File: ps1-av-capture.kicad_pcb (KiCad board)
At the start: 4 copper layers, 100 x 80 mm, 237 parts, among them J1 AV_PIGTAIL, J2 USB3_B, J3 USB_C_AUDIO, J4 JTAG, J5 UART, SW1 RESET, U1 TVP7002PZP, U10 TLV75733PDBVR, U11 TLV75533PDBVR, U12 PCM2903CDBR, U2 CYUSB3014-BZXI, U3 24LC1025-I/SN, U4 24LC1025-I/SN, U5 TPS563201DDCR, U6 TPS563201DDCR, U7 TPS563201DDCR, U8 TLV75519PDBVR, U9 TLV75519PDBVR, X1 27MHz, Y1 19.2MHz, Y2 12MHz

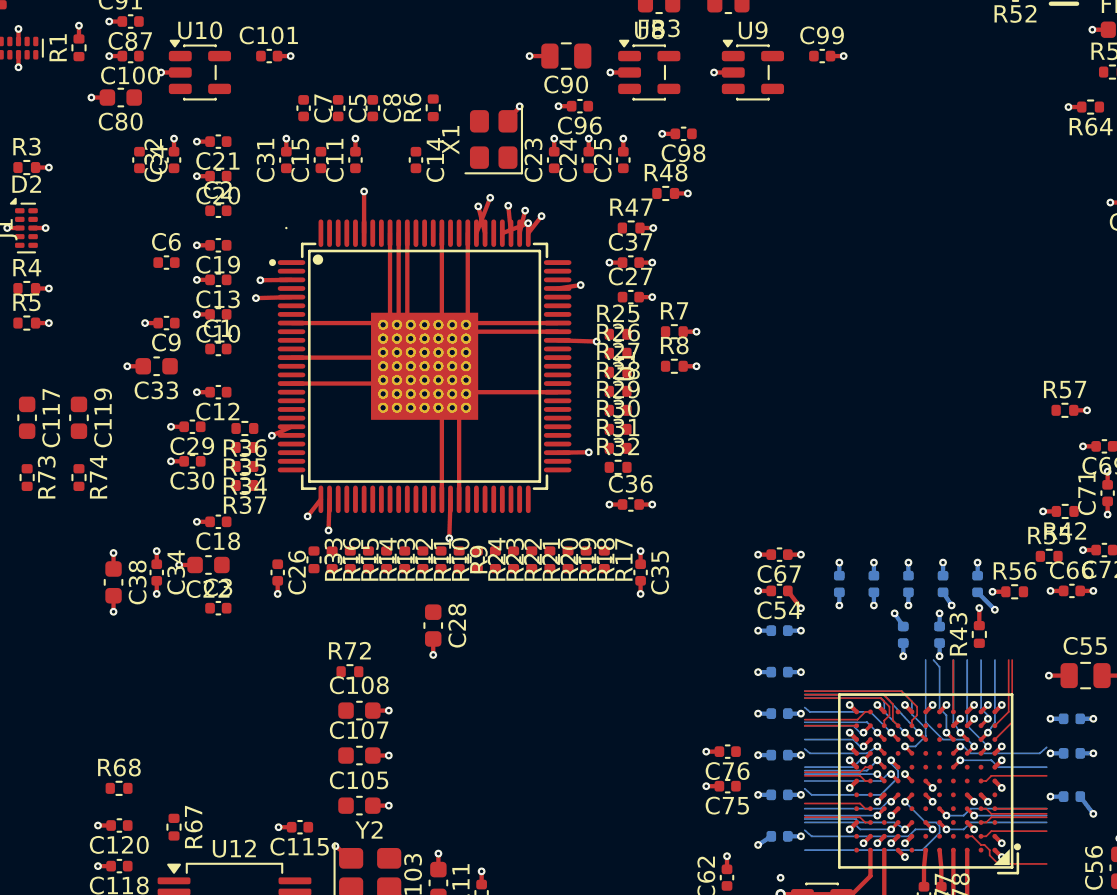
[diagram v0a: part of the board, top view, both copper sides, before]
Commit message: Layout: GPIF bundle routed, 29 of 29 VD nets TVP7002 -> FX3
The seven nets that never routed were not losing on congestion: every one
stopped after a few thousand A* expansions with the search space exhausted.
Four leave the escape box on B.Cu at x=55, 0.2 mm apart, and face the B.Cu
+1V2 decap column 1.5 mm west with its plane vias; the router allowed no
layer change inside the neckdown skirt, so they were sealed in. Vias are now
allowed there (GPIF_VIA_IN_NECK), every via keeps 0.4 mm hole-to-hole from
every other, and each escape end gets a short reserved exit.
Also: the sync 22Rs moved into the row under U1 (left of DATACLK).

DRC: no copper errors, no unconnected VD_ net. Lengths 15.5-52.5 mm.
check_geometry still flags the router's grid staircases (SHORT/ACUTE) on
these nets; cleanup is the next step.
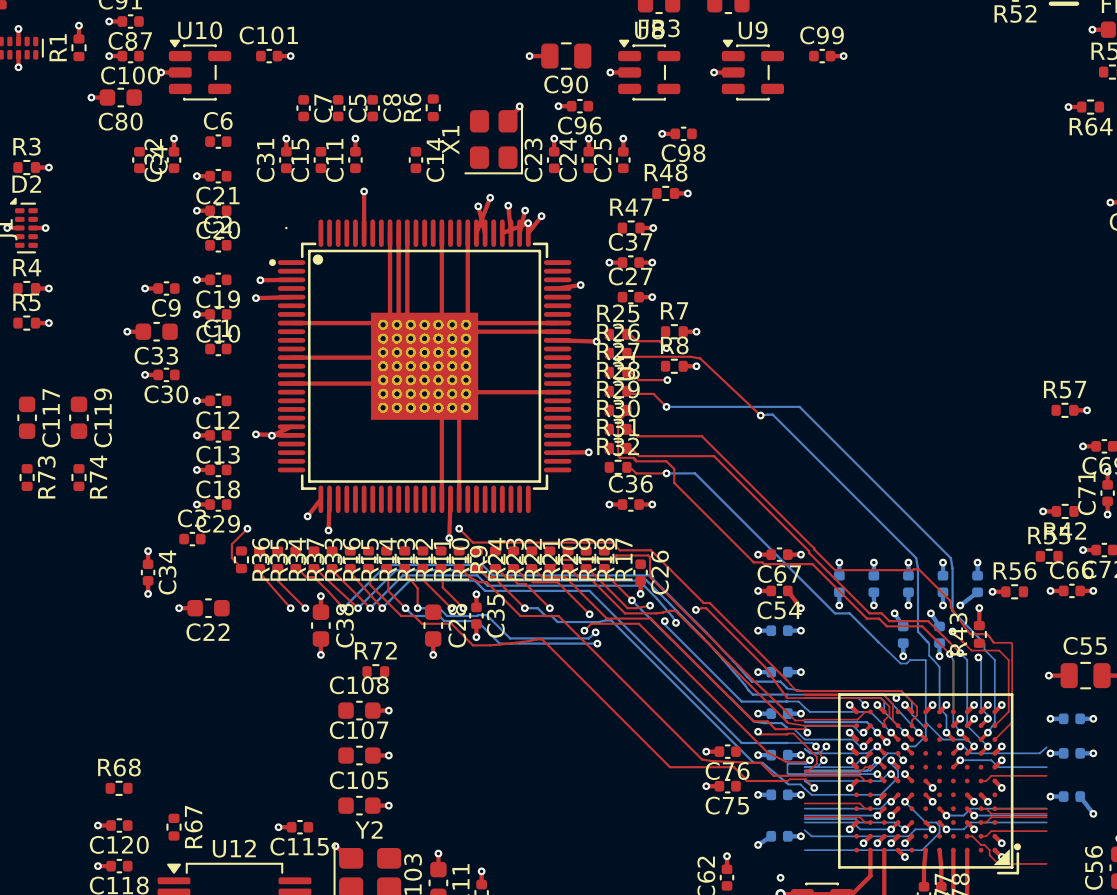
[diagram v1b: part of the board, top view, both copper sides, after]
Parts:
- moved C26 21.0 mm to (145.5, 137.9)
- moved C38 12.3 mm to (127.0, 141.0)
- moved C35 9.82 mm to (136.0, 140.4)
- moved C13 9.00 mm to (121.1, 130.0)
- moved C6 7.62 mm to (121.1, 113.0)
- moved R36 7.60 mm to (122.4, 137.2), turned to -90 degrees
- moved R35 6.56 mm to (123.5, 137.2), turned to -90 degrees
- moved R34 5.72 mm to (124.5, 137.2), turned to -90 degrees
- moved C30 5.22 mm to (118.1, 126.5)
- moved R37 5.21 mm to (125.5, 137.2), turned to -90 degrees
- moved C29 4.74 mm to (121.1, 134.0)
- moved C3 4.27 mm to (119.6, 136.0)
- moved C18 3.00 mm to (121.1, 132.0)
- moved C22 2.50 mm to (120.5, 140.0)
- moved C19 2.00 mm to (121.1, 121.0)
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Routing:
- net VD_FID: track 7.55 -> 60.1 mm, vias 1 -> 3
- net VD_HS: track 6.70 -> 52.2 mm, vias 0 -> 2
- net VD_B6: track 5.01 -> 46.5 mm, vias 1 -> 4
- net VD_VS: track 8.10 -> 46.3 mm, vias 0 -> 2
- net VD_B9: track 4.98 -> 40.8 mm, vias 1 -> 4
- net VD_B8: track 4.13 -> 38.7 mm, vias 1 -> 4
- net VD_SOG: track 10.8 -> 44.9 mm, vias 1 -> 2
- net VD_PCLK: track 8.12 -> 41.1 mm, vias 1 -> 2
- net VD_B7: track 5.73 -> 37.9 mm, vias 1 -> 2
- net VD_B5: track 3.92 -> 34.8 mm, vias 0 -> 3
- net VD_R2: track 4.13 -> 34.5 mm, vias 1 -> 3
- net VD_B3: track 4.77 -> 34.2 mm, vias 1 -> 4
- net VD_R5: track 4.89 -> 34.2 mm, vias 1 -> 2
- net VD_R4: track 4.13 -> 33.2 mm, vias 0 -> 2
- net VD_R7: track 5.01 -> 33.5 mm
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
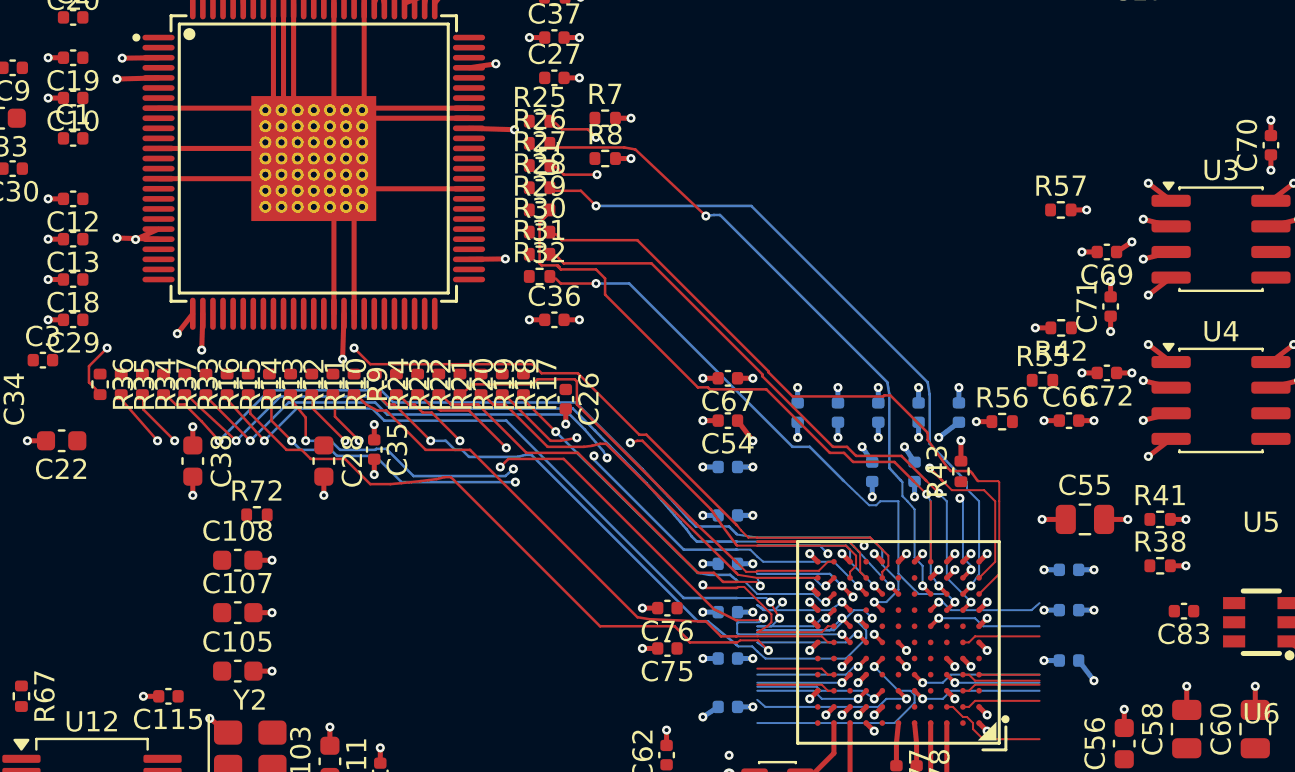
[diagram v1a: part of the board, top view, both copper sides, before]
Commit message: gpif_route: collapse grid staircases and reversals
One simplify() for both routers: vertex/staircase deletion, 45-degree corner
chamfers, neck-edge vertex kept on the edge, exact DRC-clearance checks.
Sealed escape ends branch off their stub (stub trimmed) instead of doubling back.
VD_* check_geometry: SHORT 53->7, ACUTE 17->0, OVERLAP 7->0, DANGLING 18->0;
29/29 routed, DRC 0 violations; 840.8->813.2 mm, 43->46 vias.
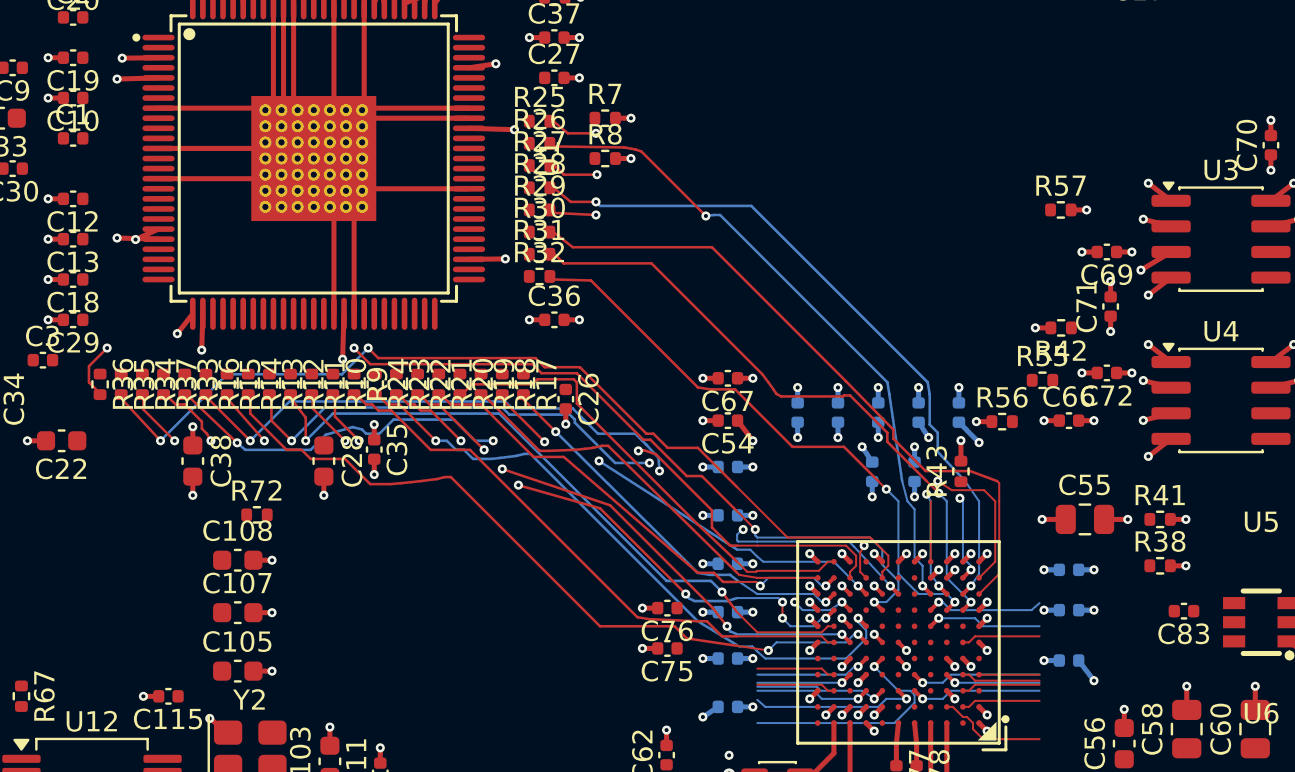
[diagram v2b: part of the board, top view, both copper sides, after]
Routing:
- net VD_FID: track 60.1 -> 48.0 mm, vias 3 -> 2
- net VD_G3: track 31.6 -> 21.3 mm, vias 3 -> 2
- net VD_B6: track 46.5 -> 36.3 mm, vias 4 -> 3
- net VD_HS: track 52.2 -> 42.6 mm
- net VD_B8: track 38.7 -> 35.2 mm, vias 4 -> 6
- net VD_B3: track 34.2 -> 30.7 mm
- net VD_R6: track 32.3 -> 29.5 mm, vias 2 -> 3
- net VD_SOG: track 44.9 -> 47.1 mm, vias 2 -> 4
- net VD_B9: track 40.8 -> 39.1 mm
- net VD_B7: track 37.9 -> 36.6 mm
- net VD_PCLK: track 41.1 -> 42.3 mm, vias 2 -> 4
- net VD_R2: track 34.5 -> 33.5 mm
- net VD_B5: track 34.8 -> 33.8 mm, vias 3 -> 2
- net VD_G8: track 27.1 -> 26.4 mm
- net VD_G6: track 24.1 -> 23.4 mm
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
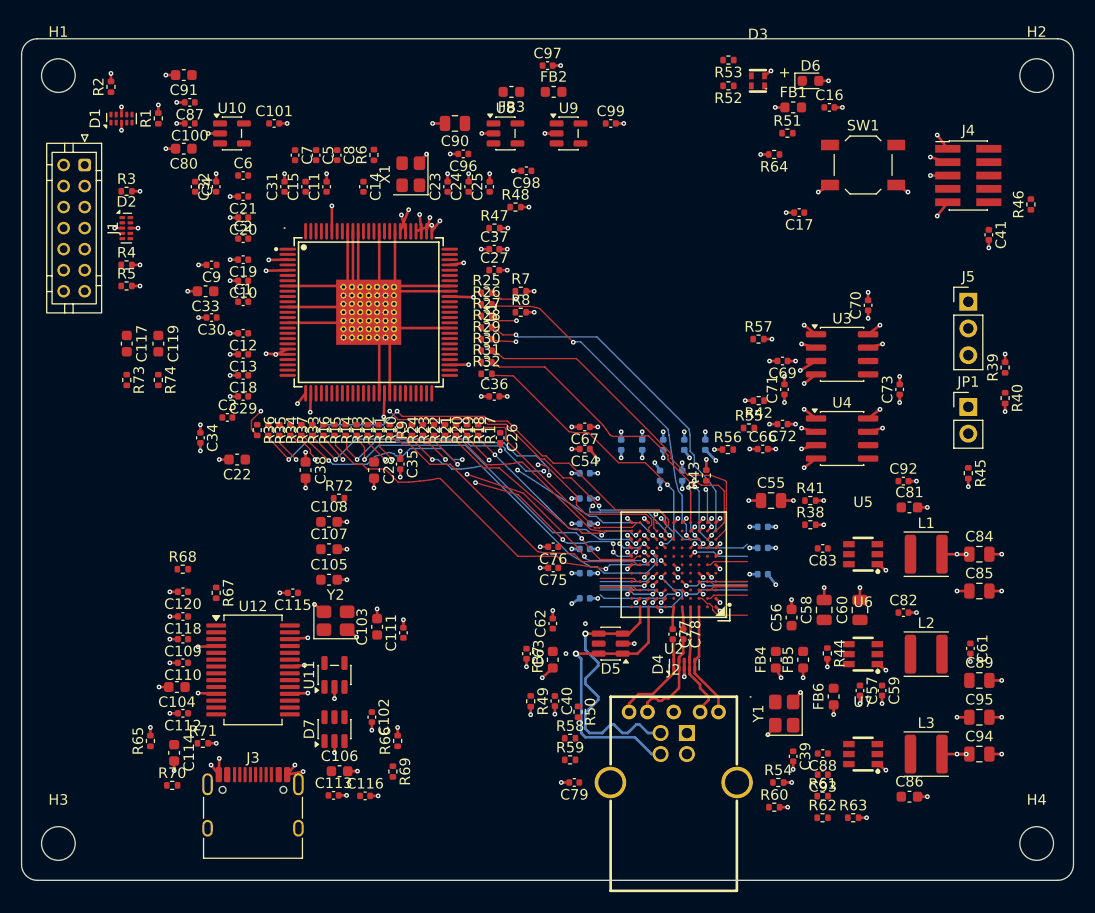
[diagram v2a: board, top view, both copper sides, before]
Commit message: fanout: one stub per plane pad
A pad that already holds a same-net via (L3/C94, L1/C84) or sits under a fanned pad
(J3 A1/B12) is left on that via; a stub may not run over a same-net via or stub.
Clears the 2 ACUTE GND and 2 OVERLAP +1V2/+3V3 findings. Unconnected 283 -> 283.
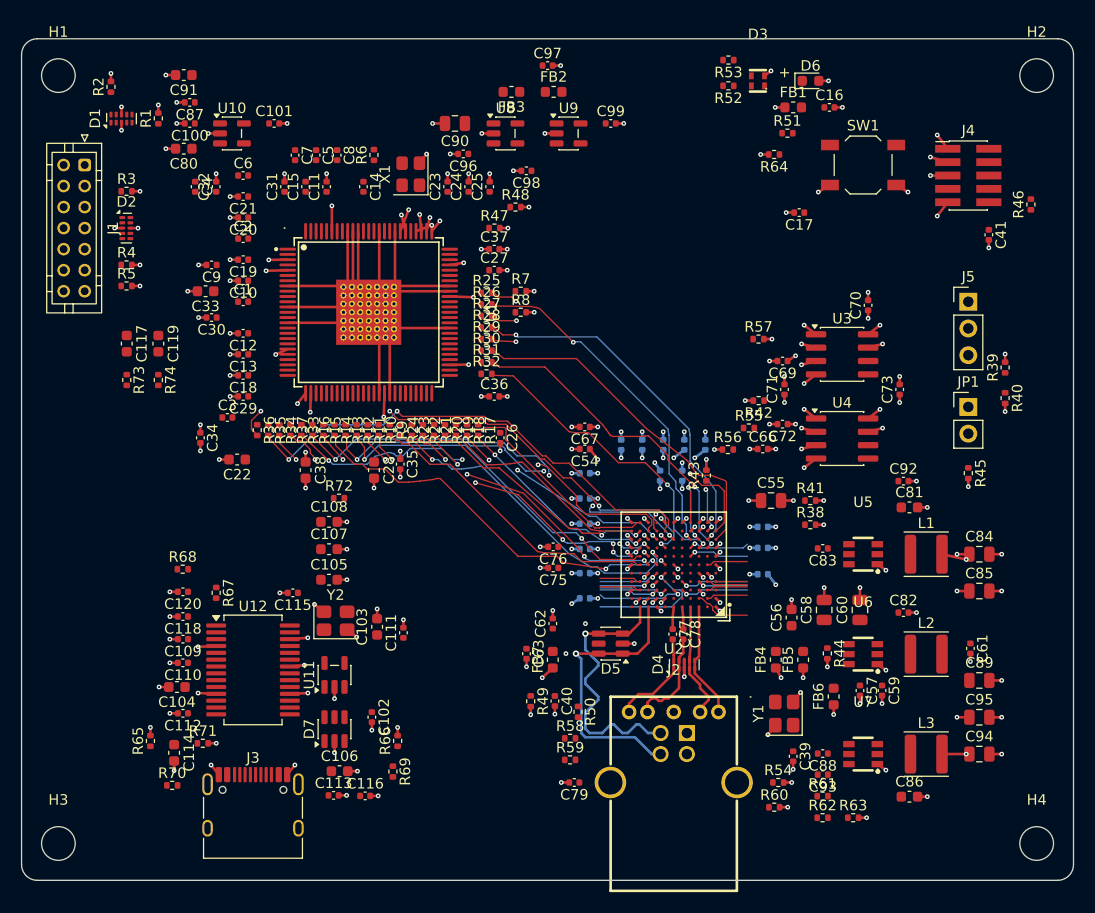
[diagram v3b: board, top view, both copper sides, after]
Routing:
- net GND: track 245.9 -> 241.0 mm, vias 194 -> 191
- net +1V2: track 23.5 -> 22.3 mm, vias 27 -> 26
- net VD_R2: track 33.5 -> 32.9 mm

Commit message: p2p_route: supplies, plane stitches, point-to-point signals
New last build stage: A* on F.Cu/B.Cu per net, FX3 supply balls dogboned first.
Unconnected 283 -> 112: supplies 105 -> 3, plane nets 13 -> 5, FX3_U3TX/RX 6 -> 0,
crystals/I2C/FSLC/22R/reset/LED/PMODE 72 -> 17. DRC 0 violations.
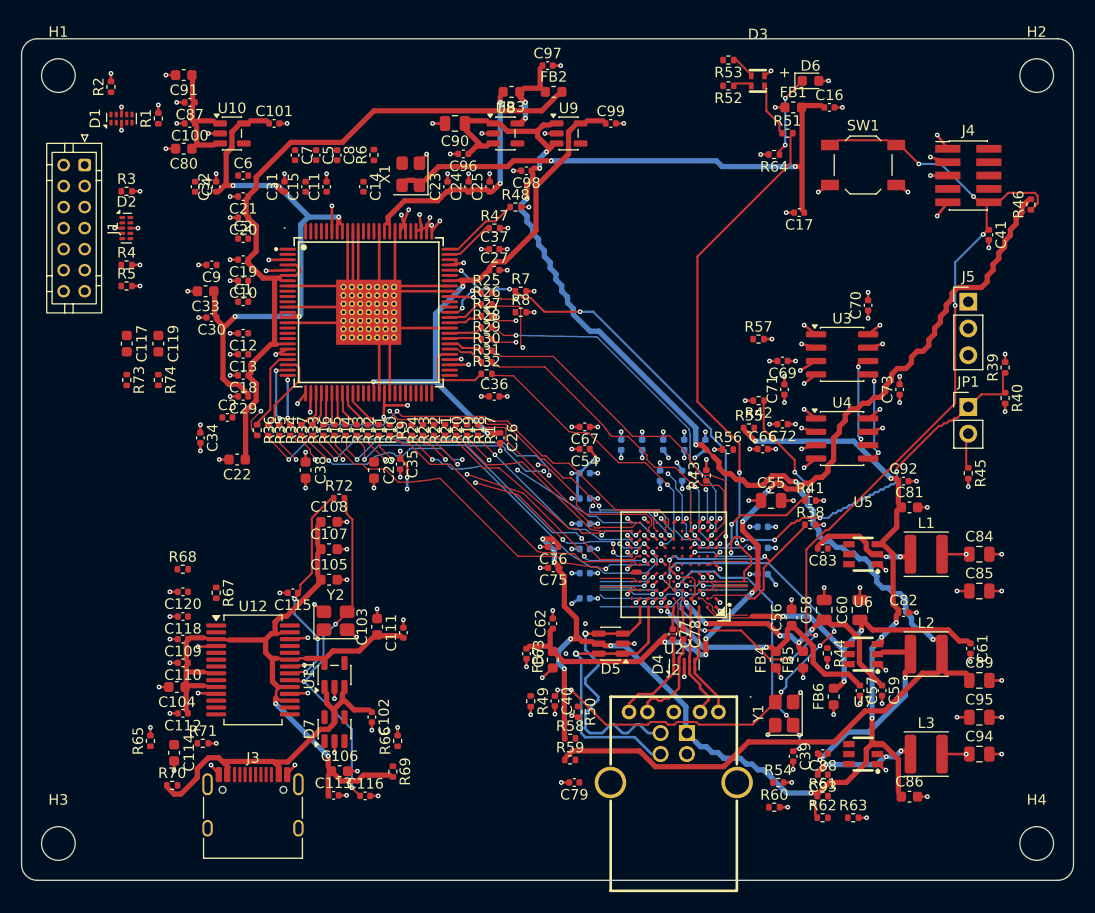
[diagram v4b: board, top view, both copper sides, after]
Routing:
- net +2V5: track 0.00 -> 126.0 mm, vias 0 -> 6
- net VBUS: track 0.00 -> 113.3 mm, vias 0 -> 11
- net FX3_CVDDQ: track 0.00 -> 87.3 mm, vias 0 -> 6
- net FX3_RESETn: track 6.53 -> 90.8 mm, vias 1 -> 8
- net TVP_AVDD: track 0.00 -> 62.8 mm
- net +3V3_AUD: track 0.00 -> 57.8 mm, vias 0 -> 2
- net FX3_XO: track 6.57 -> 58.5 mm, vias 1 -> 7
- net +3V3A: track 0.00 -> 50.0 mm, vias 0 -> 5
- net LED_R: track 3.00 -> 51.6 mm, vias 0 -> 2
- net OSC_VDD: track 0.00 -> 48.1 mm, vias 0 -> 2
- net +1V9D: track 0.00 -> 46.6 mm, vias 0 -> 3
- net TVP_RESETn: track 3.92 -> 46.7 mm, vias 0 -> 4
- net FX3_PMODE0: track 5.73 -> 38.8 mm, vias 1 -> 6
- net FX3_U3RX: track 0.00 -> 31.7 mm, vias 0 -> 3
- net AUD_XO: track 0.00 -> 30.8 mm, vias 0 -> 3
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
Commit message: gpif_route: VD_HS escapes north, bundle kept off In2 planes
VD_HS leaves K8 north on F.Cu (38.1 mm, 0 vias; was west, 41.2 mm, 2 vias). In2 is
closed to the bundle over +1V2/+3V3 outside the escape box; F.Cu U1->22R paths kept clear.
vs a fresh 49b060d build: GPIF 29/29 both, DRC 0 copper, unconnected 111 -> 96,
In2 breaks >=0.25 mm2 +1V2 5 -> 1, +3V3 4 -> 1, VD_ SHORT 5 -> 2. TVP_HSOUT now unrouted.
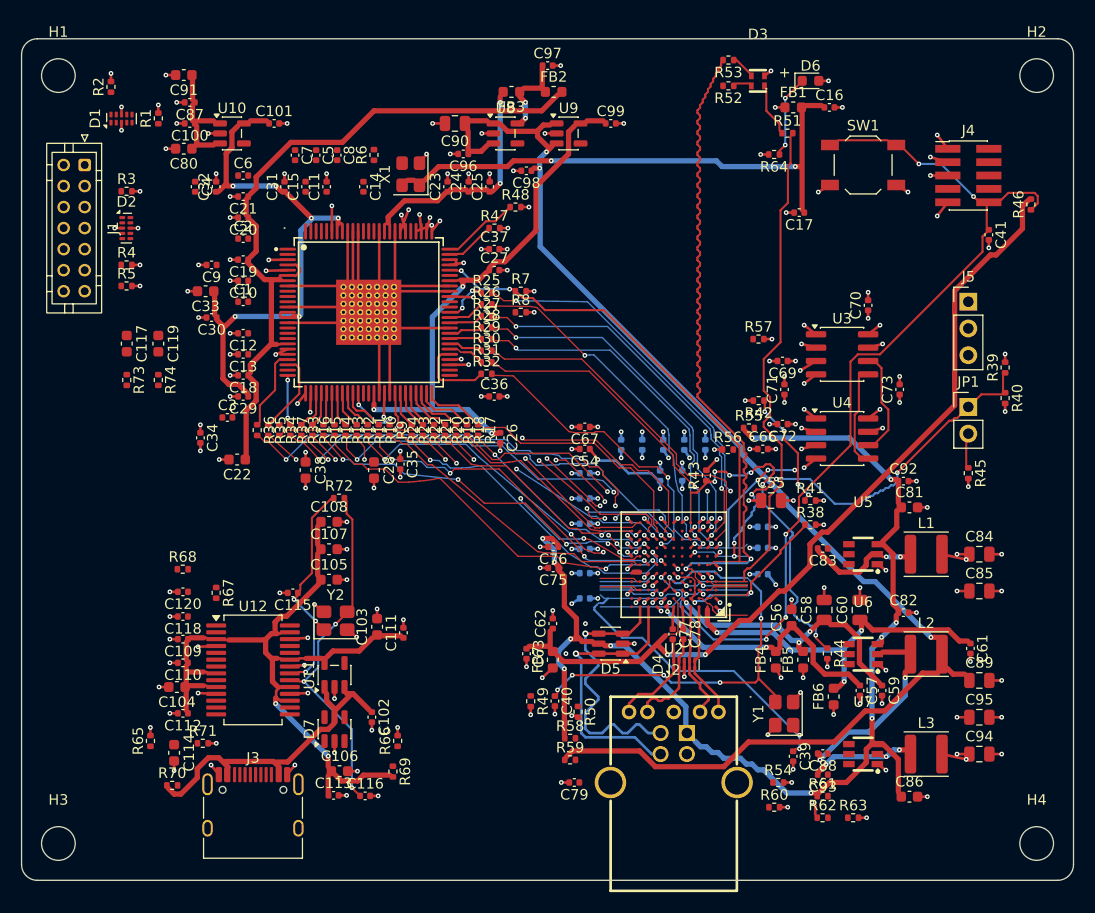
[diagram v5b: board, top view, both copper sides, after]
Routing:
- net LED_B: track 4.77 -> 70.1 mm, vias 1 -> 3
- net FX3_PMODE2: track 3.00 -> 33.4 mm, vias 0 -> 6
- net FX3_XO: track 58.5 -> 49.1 mm
- net +2V5: track 126.0 -> 118.3 mm, vias 6 -> 3
- net FX3_FSLC: track 29.3 -> 22.8 mm, vias 4 -> 3
- net FX3_CVDDQ: track 87.3 -> 81.7 mm, vias 6 -> 2
- net TVP_HSOUT: track 5.39 -> 0.00 mm, vias 2 -> 0
- net VD_R2: track 33.8 -> 39.1 mm, vias 3 -> 4
- net TVP_G2: track 0.00 -> 4.94 mm
- net TVP_B2: track 0.00 -> 4.57 mm, vias 0 -> 2
- net TVP_G3: track 0.00 -> 4.48 mm
- net FX3_RESETn: track 90.8 -> 86.5 mm, vias 8 -> 6
- net TVP_G4: track 0.00 -> 4.00 mm
- net +1V2: track 27.2 -> 31.1 mm, vias 27 -> 28
- net VD_PCLK: track 42.3 -> 45.9 mm, vias 4 -> 6
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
